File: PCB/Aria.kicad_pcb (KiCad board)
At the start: 4 copper layers, 80 x 27 mm, 90 parts, among them J1 B2B-PH-K-S(LF)(SN), J2 B3B-PH-K-S(LF)(SN), J3 20021121-00010C4LF, J4 0475890001-MicroUSBPort, P1 CONN_01X18, P2 CONN_01X18, Q1 DMG2307L-7, Q2 DMG2307L-7, SW1 B3U-1000P, SW2 B3U-1000P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

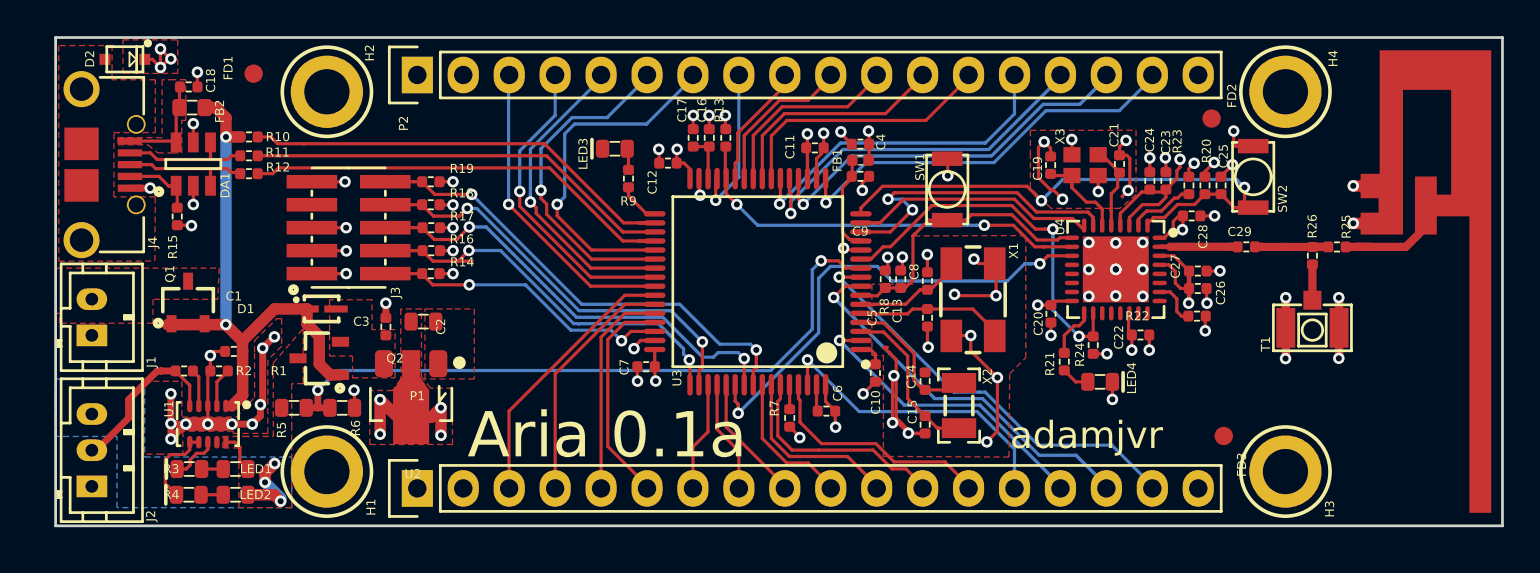
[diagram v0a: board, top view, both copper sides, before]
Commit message: ESP Footprint Error and RF improvement
ESP8285 footprint was wrong, made when I was still learning kiCAD.
Footprint change and entire topology reconstructed and rerouted. Added
ground pours and heavy via stitching to improve RF performance. Also
started an ESP-12E module based variant. Both will be fabbed at the same
time.
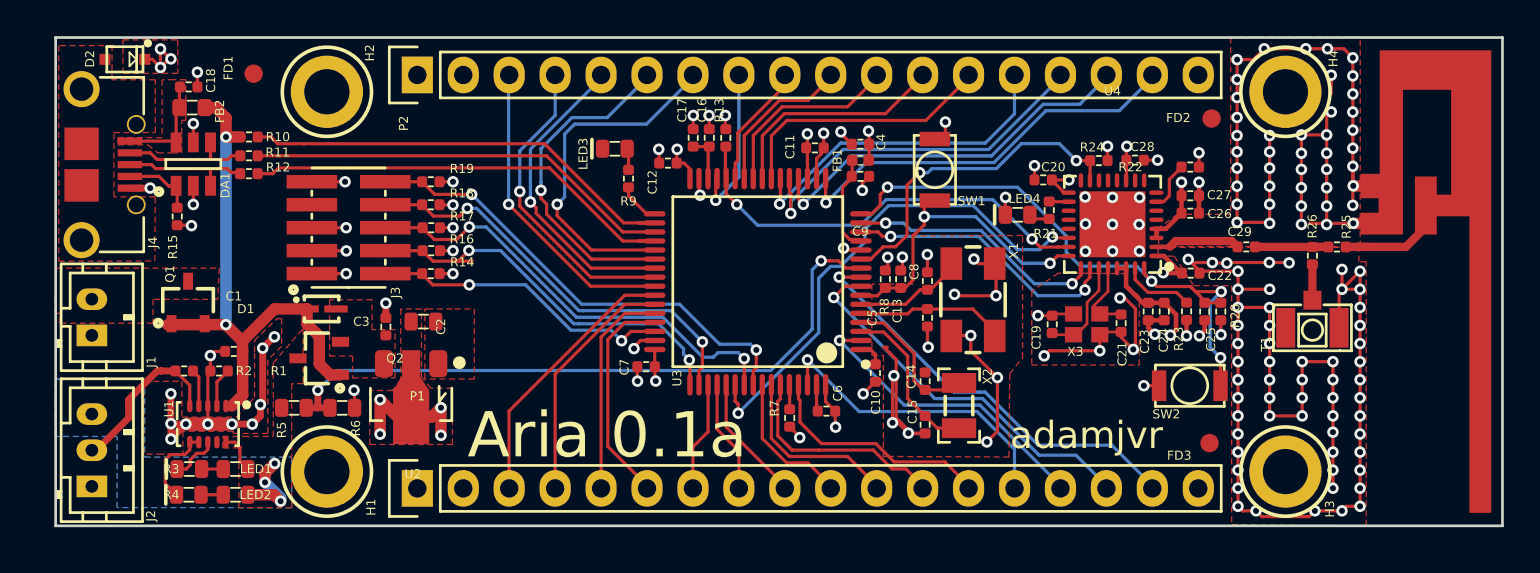
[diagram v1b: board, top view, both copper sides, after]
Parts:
- moved SW2 12.1 mm to (208.6, 90.8), turned to 0 degrees
- moved LED4 10.3 mm to (199.1, 81.4), turned to 180 degrees
- moved R24 10.2 mm to (203.6, 78.4), turned to 180 degrees
- moved C19 8.80 mm to (201.0, 87.4)
- moved X3 8.80 mm to (202.9, 87.4)
- moved C21 8.80 mm to (204.8, 87.4), turned to 270 degrees
- moved R21 8.41 mm to (200.8, 81.1), turned to 270 degrees
- moved R22 8.25 mm to (208.6, 78.7)
- moved C20 7.42 mm to (200.5, 79.5), turned to 180 degrees
- moved C23 7.29 mm to (206.3, 86.7), turned to 270 degrees
- moved C24 7.27 mm to (207.2, 86.7), turned to 270 degrees
- moved C25 7.03 mm to (209.4, 86.7), turned to 270 degrees
- moved R20 7.03 mm to (210.3, 86.7), turned to 270 degrees
- moved R23 6.96 mm to (208.4, 86.7), turned to 90 degrees
- moved C22 4.40 mm to (208.6, 84.6)
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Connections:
- R21 pad 1: Net-(LED4-Pad1) -> Net-(R21-Pad1)
- R21 pad 2: Net-(R21-Pad2) -> Net-(LED4-Pad1)
- U4 pad 16: Net-(R21-Pad2) -> Net-(U4-Pad16)
- U4 pad 18: Net-(U4-Pad18) -> Net-(R21-Pad1)
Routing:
- net GND: track 131.0 -> 233.0 mm, vias 82 -> 172
- net +3V3: track 51.8 -> 46.3 mm
- net /MCU_STM32F446RET6/ESP_URX: track 18.1 -> 15.3 mm
- net Net-(R21-Pad2): track 2.81 -> 0.00 mm
- net /MCU_STM32F446RET6/ESP_PGM_MODE: track 21.0 -> 18.4 mm
- net /MCU_STM32F446RET6/ESPTOST_BOOT0: track 26.2 -> 28.2 mm
- net /MCU_STM32F446RET6/ESP_ST_RST: track 15.5 -> 17.1 mm, vias 0 -> 2
- net /MCU_STM32F446RET6/STM_ESP_RST: track 31.4 -> 32.6 mm, vias 2 -> 4
- net Net-(R21-Pad1): track 0.00 -> 1.08 mm
- net /MCU_STM32F446RET6/ESPTOST_BOOT1: track 22.8 -> 23.7 mm
- net /MCU_STM32F446RET6/ESP_UTX: track 13.7 -> 14.1 mm, vias 0 -> 2
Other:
- net class Default: clearance 0.1778 -> 0.1524
- rule trace_clearance: 0.1778 -> 0.1524
- rule trace_min: 0.1778 -> 0.1524

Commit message: DRC Cleared and Pictures
DRC cleared of errors for both Aria board designs. New pictures have
been added. Readme has also been updated.
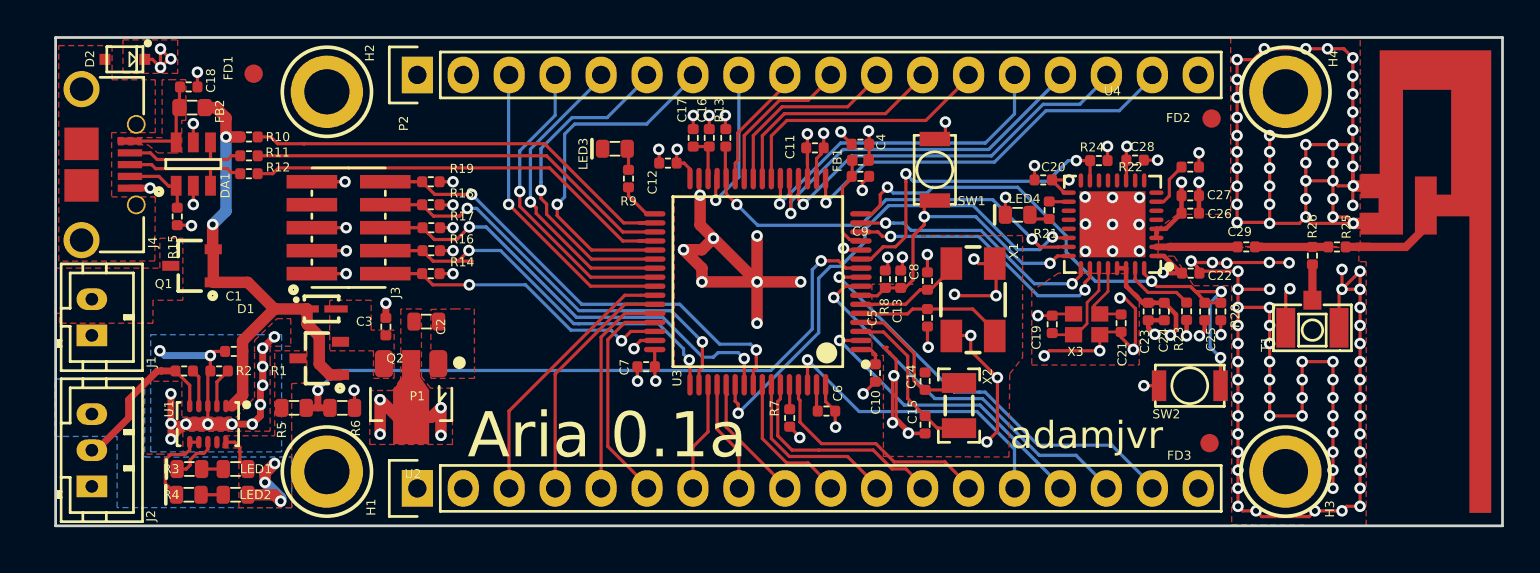
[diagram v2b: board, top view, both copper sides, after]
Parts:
- moved Q1 2.04 mm to (153.4, 84.2), turned to 180 degrees
- moved C3 0.16 mm to (166.4, 87.3)
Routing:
- net GND: track 233.0 -> 262.4 mm, vias 172 -> 179
- net /MCU_STM32F446RET6/VBUS: track 31.4 -> 28.9 mm
- added copper zone on B.Cu, net GND

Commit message: Switch
Power switch added for switching board off for storage and shipping.
Power supply circuit routing revised and updated.
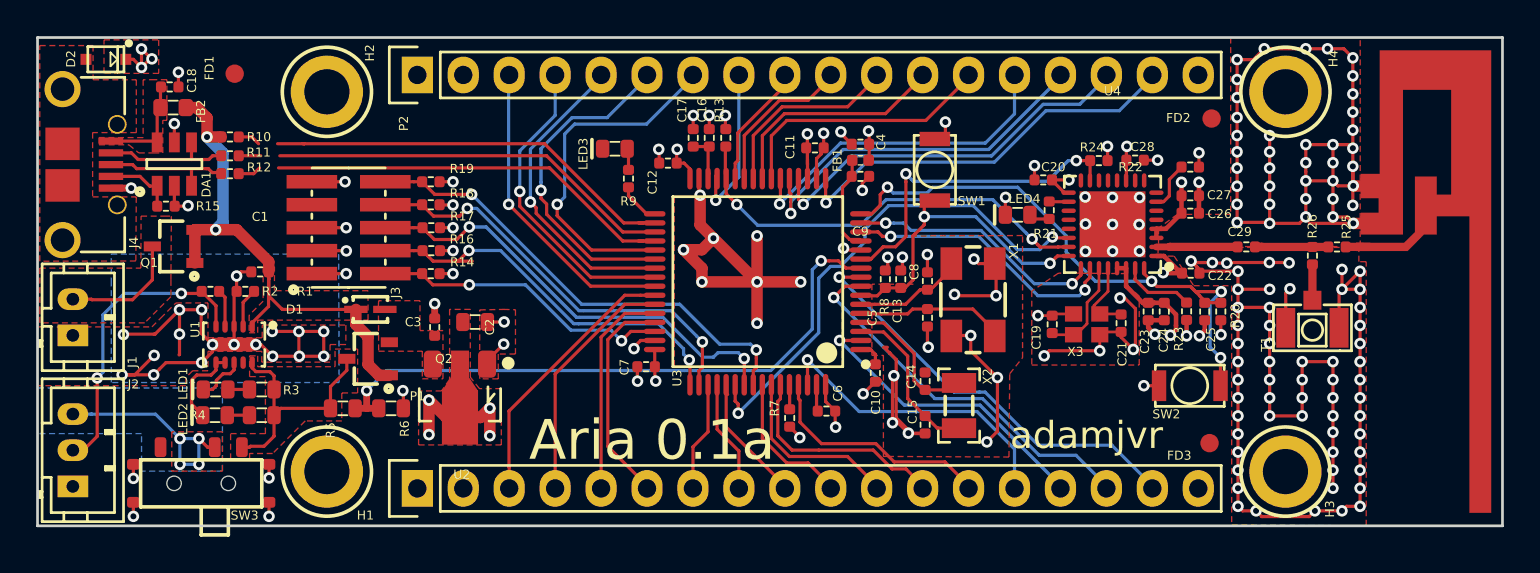
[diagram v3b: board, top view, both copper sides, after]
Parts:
- added SW3: CUS-12TB, PCB_Footprints:CUS-12TB, F.Cu at (153.9, 96.2)
- moved R4 4.63 mm to (157.3, 92.5)
- moved LED2 4.63 mm to (154.7, 92.5)
- moved C1 4.63 mm to (157.2, 84.5)
- moved LED1 4.63 mm to (154.7, 91.0)
- moved R2 4.63 mm to (154.4, 85.6)
- moved R3 4.63 mm to (157.3, 91.0)
- moved U1 4.63 mm to (155.7, 88.6)
- moved R1 4.63 mm to (156.4, 85.6)
- moved D1 2.70 mm to (163.3, 86.6)
- moved R5 2.70 mm to (161.8, 92.1)
- moved R6 2.70 mm to (164.4, 92.1)
- moved U2 2.70 mm to (168.2, 91.5)
- moved C2 2.70 mm to (166.8, 87.6)
- moved C3 2.70 mm to (169.1, 87.3)
- moved Q2 2.70 mm to (163.2, 89.3)
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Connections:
- J2 pad 3: /Power/BAT -> Net-(J2-Pad3)
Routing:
- net GND: track 262.4 -> 280.4 mm, vias 179 -> 188
- net Net-(J2-Pad3): track 0.00 -> 12.5 mm, vias 0 -> 4
- net /Power/THERM: track 9.31 -> 17.0 mm, vias 0 -> 2
- net Net-(J1-Pad2): track 0.00 -> 6.71 mm
- net /Power/BAT: track 6.90 -> 13.4 mm, vias 3 -> 0
- net /MCU_STM32F446RET6/BAT_VOLT: track 37.4 -> 34.7 mm
- net /MCU_STM32F446RET6/VBUS: track 28.9 -> 30.7 mm
- added copper zone on F.Cu, net /MCU_STM32F446RET6/VBUS
- added copper zone on B.Cu, net Net-(J2-Pad3)
- added copper zone on F.Cu, net Net-(J2-Pad3)
- removed copper zone on B.Cu, net /Power/BAT
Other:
- board size 80 x 27 mm -> 81 x 27 mm

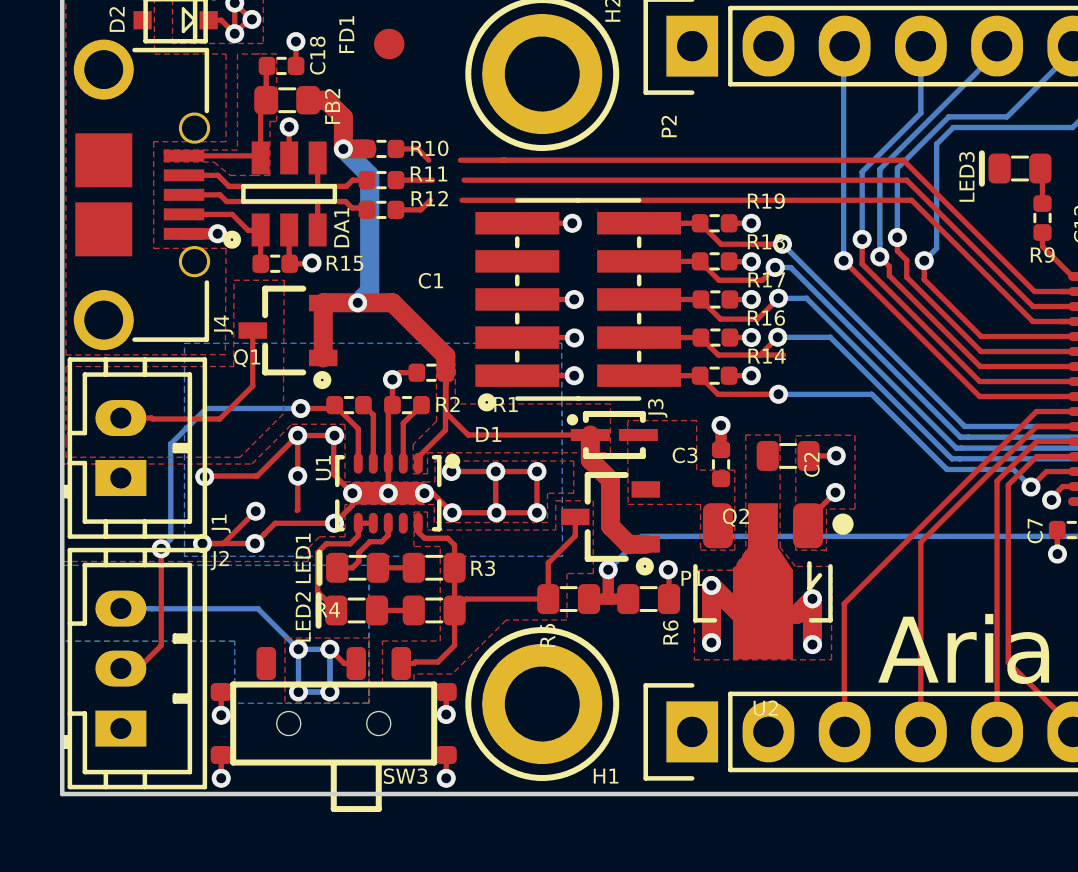
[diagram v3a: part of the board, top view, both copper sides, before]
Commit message: Power Switch Revision
Power switch and power supply topology revised. New microchip LDO from
Ventor replaces old LDO, power switch not toggles LDO shutdown enable
for turing Aria on and off.
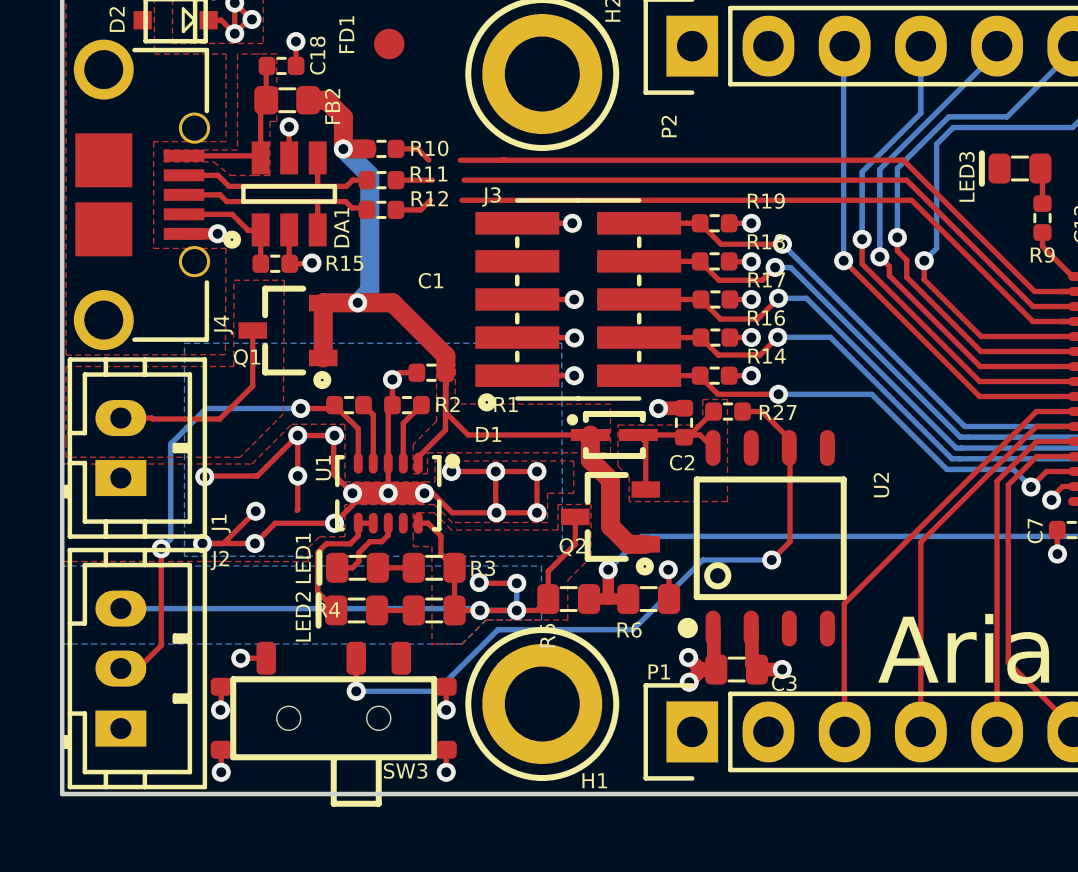
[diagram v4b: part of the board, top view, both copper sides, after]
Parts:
- added R27: RC1005F103CS, PCB_Footprints:R0402, F.Cu at (167.1, 85.8)
- U2: value AZ1117CR-3.3TRG1_1 -> TC1265-3.3VOA; footprint PCB_Footprints:AZ1117CR-3.3TRG1 -> PCB_Footprints:TC1265-3.3VOA
- moved C3 7.32 mm to (167.4, 94.4)
- moved C2 1.86 mm to (165.6, 86.2)
- moved U2 1.45 mm to (168.5, 90.1), turned to 90 degrees
- moved SW3 0.17 mm to (153.9, 96.1)
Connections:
- C2 pad 1: Net-(C2-Pad1) -> /Power/LDO_VIN
- D1 pad 2: Net-(C2-Pad1) -> /Power/LDO_VIN
- J2 pad 3: Net-(J2-Pad3) -> /Power/BAT
- Q2 pad 2: Net-(C2-Pad1) -> /Power/LDO_VIN
- SW3 pad 1: Net-(SW3-Pad1) -> GND
- SW3 pad 2: Net-(J2-Pad3) -> Net-(R27-Pad2)
- SW3 pad 3: /Power/BAT -> Net-(SW3-Pad3)
- U2 pad 1: GND -> +3V3
- U2 pad 2: +3V3 -> GND
- U2 pad 3: Net-(C2-Pad1) -> Net-(U2-Pad3)
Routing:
- net Net-(R27-Pad2): track 0.00 -> 23.1 mm, vias 0 -> 2
- net Net-(J2-Pad3): track 12.5 -> 0.00 mm, vias 4 -> 0
- net /Power/BAT: track 13.4 -> 25.4 mm, vias 0 -> 4
- net /Power/LDO_VIN: track 0.00 -> 5.93 mm
- net +3V3: track 46.3 -> 42.5 mm, vias 25 -> 23
- net /MCU_STM32F446RET6/SWCLK_TCK: track 22.4 -> 21.4 mm
- net GND: track 280.4 -> 281.2 mm, vias 188 -> 187
- added copper zone on B.Cu, net /Power/BAT
- added copper zone on F.Cu, net /Power/LDO_VIN
- removed copper zone on F.Cu, net +3V3
- removed copper zone on F.Cu, net Net-(C2-Pad1)
- removed copper zone on B.Cu, net Net-(J2-Pad3)
- removed copper zone on F.Cu, net Net-(J2-Pad3)
